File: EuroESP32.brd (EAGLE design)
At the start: 50.8 x 86.4 mm, 127 parts, among them IC1 TL074D, IC10 MCP6004, IC2 TL072, IC3 TL072, IC4 WM8731, IC5 TL074D, IC7 ADP7118, P4 POWER_SIMPLE10, U1 LM4040SOT23, U2 MCP3204-CI/SL

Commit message: Plaquette redimensionnée
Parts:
- removed H2: PCB_SCREW, parts_aman:PCB_SCREW
- moved CVOUT4 103.4 mm to (101.0, -24.1), turned to 90 degrees
- moved CVOUT3 101.8 mm to (98.4, -24.1), turned to 90 degrees
- moved CVOUT2 100.3 mm to (95.9, -24.1), turned to 90 degrees
- moved CVOUT1 99.0 mm to (93.4, -24.1), turned to 90 degrees
- moved CVIN(100K)3 97.7 mm to (90.8, -24.1), turned to 90 degrees
- moved CVIN(100K)2 96.5 mm to (88.3, -24.1), turned to 90 degrees
- moved CVIN(100K)1 95.5 mm to (85.7, -24.1), turned to 90 degrees
- moved CVIN(100K)0 94.6 mm to (83.2, -24.1), turned to 90 degrees
- moved J_ROUT 93.8 mm to (80.7, -24.1), turned to 90 degrees
- moved J_LOUT 93.2 mm to (78.1, -24.1), turned to 90 degrees
- moved J_RIN 92.7 mm to (75.6, -24.1), turned to 90 degrees
- moved +3.3VA 92.6 mm to (60.3, -24.1), turned to 90 degrees
- moved J_LIN 92.3 mm to (73.0, -24.1), turned to 90 degrees
- moved +12V 92.3 mm to (62.9, -24.1), turned to 90 degrees
- moved -10VREF 92.1 mm to (70.5, -24.1), turned to 90 degrees
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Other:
- board size 50.8 x 86.4 mm -> 108 x 30 mm

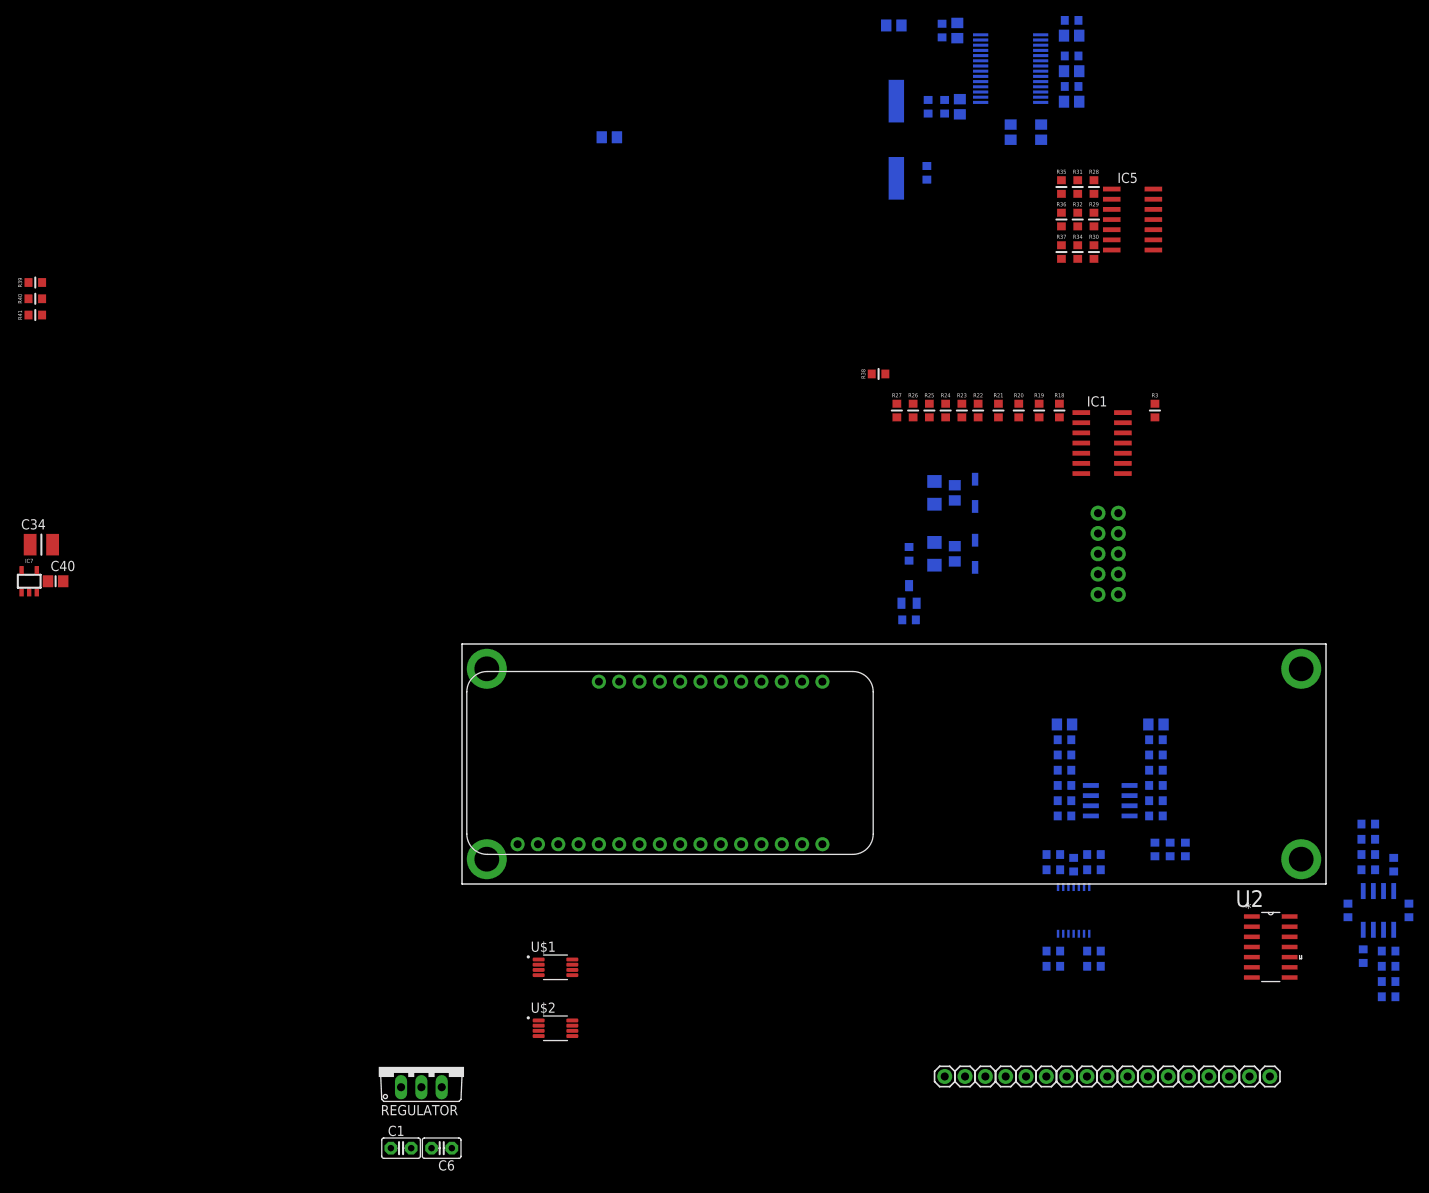
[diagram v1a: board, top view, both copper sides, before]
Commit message: v0.1
TODO : TLC for the Labels
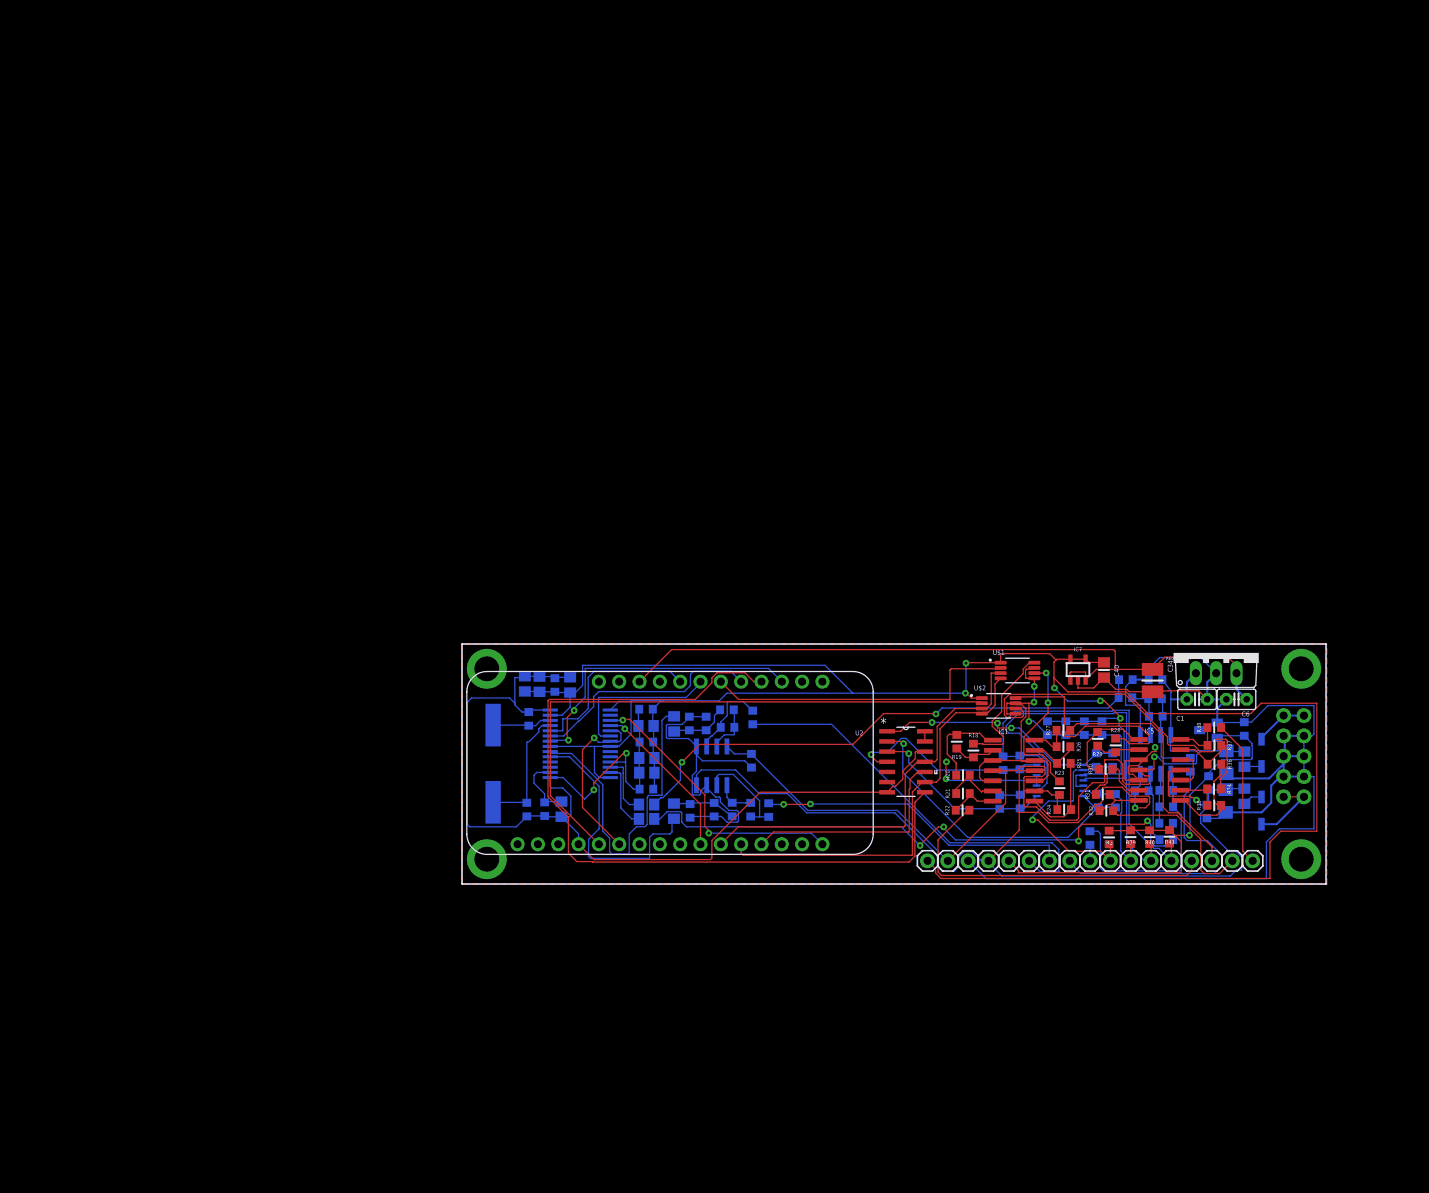
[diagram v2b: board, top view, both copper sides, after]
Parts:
- -10VREF: value -10VREF -> -10V
- CVIN(100K)0: value CVIN(100k)0 -> CVI0
- CVIN(100K)1: value CVIN(100K)1 -> CVI1
- CVIN(100K)2: value CVIN(100K)2 -> CVI2
- CVIN(100K)3: value CVIN(100K)3 -> CVI3
- CVOUT1: value CVOUT1 -> CVO1
- CVOUT2: value CVOUT2 -> CVO2
- CVOUT3: value CVOUT3 -> CVO3
- CVOUT4: value CVOUT4 -> CVO4
- moved R41 156.0 mm to (88.4, 5.91), turned to 90 degrees
- moved R40 154.7 mm to (85.9, 5.86), turned to 90 degrees
- moved R39 153.5 mm to (83.6, 5.86), turned to 90 degrees
- moved C34 139.9 mm to (86.3, 25.4), turned to 270 degrees
- moved IC7 131.6 mm to (77.0, 26.8)
- moved C40 131.5 mm to (80.2, 26.8), turned to 270 degrees
- moved C1 114.2 mm to (91.9, 23.1)
- moved C6 114.1 mm to (96.8, 23.1)
- moved REGULATOR 112.0 mm to (94.3, 28.9)
- moved C30 102.7 mm to (23.1, 11.9), turned to 180 degrees
- moved C15 101.4 mm to (23.0, 19.8), turned to 0 degrees
- moved C16 101.2 mm to (23.0, 21.9), turned to 0 degrees
- moved C14 101.0 mm to (10.3, 9.36)
- moved C23 100.9 mm to (23.1, 15.8), turned to 180 degrees
- moved C11 100.9 mm to (12.4, 9.36)
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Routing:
- net GND: track 0.00 -> 461.1 mm, vias 0 -> 8
- net +3.3VA: track 0.00 -> 294.9 mm, vias 0 -> 5
- net -12V: track 0.00 -> 149.2 mm, vias 0 -> 2
- net +12V: track 0.00 -> 126.4 mm, vias 0 -> 1
- net ADC_CS: track 0.00 -> 101.6 mm
- net 5V: track 0.00 -> 92.6 mm
- net N$49: track 0.00 -> 76.5 mm, vias 0 -> 4
- net DAC34_CS: track 0.00 -> 74.3 mm
- net N$57: track 0.00 -> 67.2 mm, vias 0 -> 2
- net -10VREF: track 0.00 -> 59.4 mm, vias 0 -> 1
- net N$15: track 0.00 -> 54.7 mm
- net SPI_MOSI: track 0.00 -> 52.8 mm
- net SPI_CLK: track 0.00 -> 52.3 mm
- net N$21: track 0.00 -> 51.9 mm
- net N$1: track 0.00 -> 51.8 mm
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- added copper zone on layer 1, net GND
- added copper zone on layer 16, net GND
